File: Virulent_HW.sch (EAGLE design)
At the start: 74 parts, among them SW1 COM08229, SW2 COM08720, U1 STM32F050G6U6

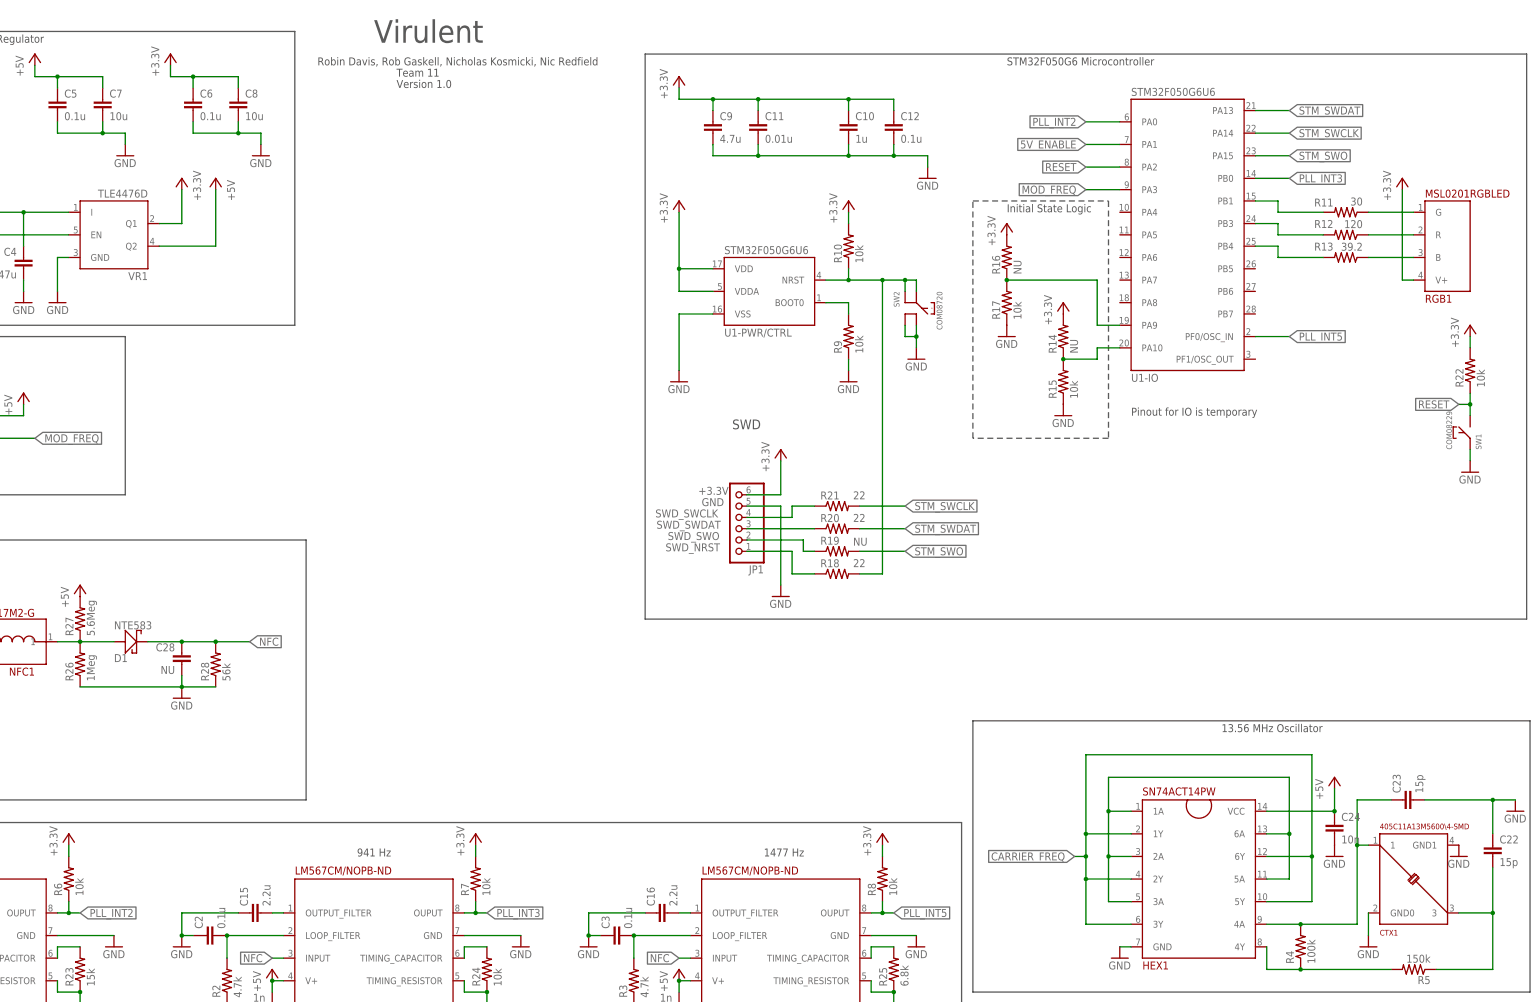
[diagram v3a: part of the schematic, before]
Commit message: Updated uC pinout.
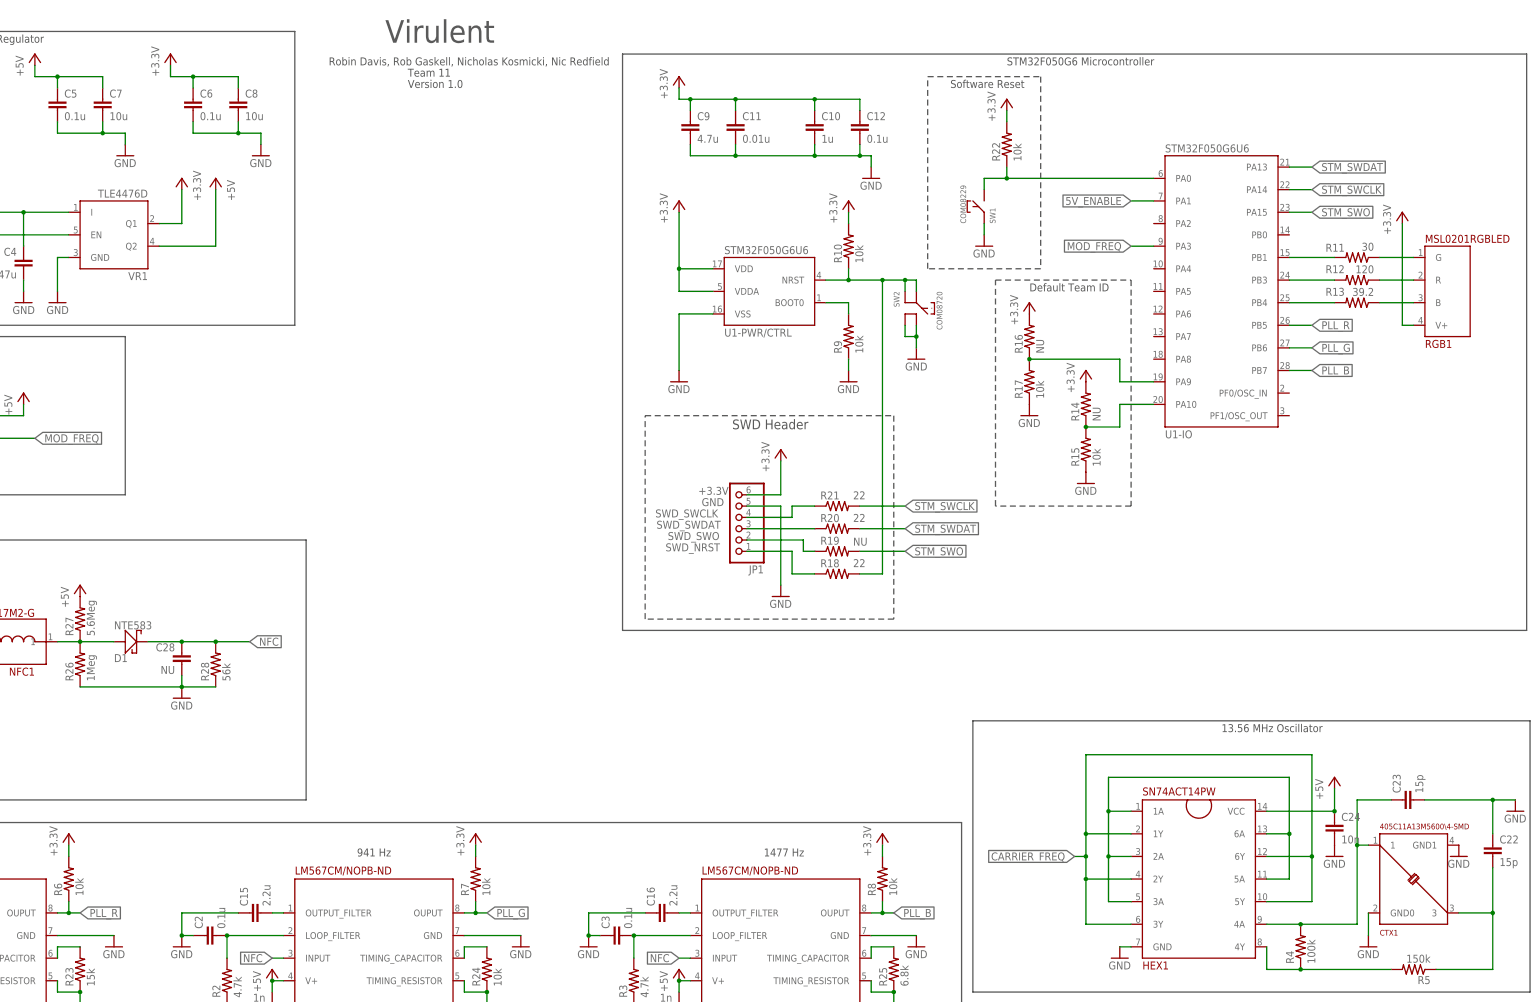
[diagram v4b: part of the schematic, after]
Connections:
- net N$11 renamed LED_GREEN
- net N$15 renamed LED_RED
- net N$16 renamed LED_BLUE
- net N$21 renamed O_GREEN
- net N$22 renamed O_RED
- net N$23 renamed O_BLUE
- net N$25 renamed TEAMID1
- net N$28 renamed TEAMID0
- removed net PLL_INT2: PLL1.OUPUT@8, R6.1, U1-IO.PA0@6
- removed net PLL_INT3: PLL2.OUPUT@8, R7.1, U1-IO.PB0@14
- removed net PLL_INT5: PLL3.OUPUT@8, R8.1, U1-IO.PF0/OSC_IN@2
- removed net RESET: R22.1, SW1.2@2, U1-IO.PA2@8
- new net NRESET_SOFT: R22.1, SW1.2@2, U1-IO.PA0@6
- new net PLL_B: PLL3.OUPUT@8, R8.1, U1-IO.PB7@28
- new net PLL_G: PLL2.OUPUT@8, R7.1, U1-IO.PB6@27
- new net PLL_R: PLL1.OUPUT@8, R6.1, U1-IO.PB5@26
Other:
- note added: "Default Team ID"
- note added: "SWD Header"
- note added: "Software Reset"
- note removed: "Initial State Logic"
- note removed: "Pinout for IO is temporary"
- note removed: "SWD"
- moved on the sheet: C10, C11, C12, C9, R11, R12, R13, R14, R15, R16, R17, R22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

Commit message: updated cap sizes. Started to mess with board layour but did not accomplish very much.
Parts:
- added C30: 0.1u, rcl:C-EUC0402
- added R31: 10k, Virulent_HW:R-US_R0402
- C1, C14, C15, C16, C17, C18, C19, C2, C20, C21, C22, C23, C24, C25, C27, C28, C29, C3: device rcl:C-EUC1206 -> rcl:C-EUC0402
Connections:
- removed net CARRIER_FREQ: HEX1.1Y@2, HEX1.2Y@4, HEX1.3Y@6, HEX1.5Y@10, HEX1.6Y@12, SPST1.A@1
- new net CHOPPED_FREQ: C24.1, HEX1.VCC@14, SPST1.B@2
- new net N$11: C30.2, SPST1.VCC@5
- net +5V: now also C30.1, SPST1.A@1; no longer C24.1, HEX1.VCC@14, SPST1.VCC@5
- net 5V_ENABLE: now also R31.2
- net GND: now also R31.1
- net NFC: now also HEX1.1Y@2, HEX1.2Y@4, HEX1.3Y@6, HEX1.5Y@10, HEX1.6Y@12; no longer SPST1.B@2
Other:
- note added: "Frequency Generation"
- note added: "NFC"
- note removed: "13.56 MHz Oscillator"
- note removed: "Frequency Modulation"
- note removed: "Receiver"
- moved on the sheet: C10, C11, C12, C22, C23, C24, C25, C28, C29, C9, CT1, CTX1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

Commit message: messed around with PCB layout
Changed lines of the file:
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@@
 <pinref part="R5" gate="G$1" pin="2"/>
 <wire x1="88.9" y1="114.3" x2="109.22" y2="114.3" width="0.1524" layer="91"/>
+<junction x="109.22" y="127"/>
 </segment>
 </net>
@@
 <pinref part="C24" gate="G$1" pin="1"/>
 <wire x1="48.26" y1="162.56" x2="101.6" y2="162.56" width="0.1524" layer="91"/>
-</segment>
-</net>
+<junction x="101.6" y="162.56"/>
+</segment>
+</net>

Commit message: First Draft of PCB. Changes made to reciever of schematic per Nic's instructions.Changed LED pins to better suit routing needs. Added dpdt switch to change nfc coil from tx/rx, to be controlled by microcontroller. Added user's momentary push-button
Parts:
- removed D1: NTE583, Virulent_HW:NTE583
- added C31, C35: 1n, rcl:C-EUC0402
- added C32, C33, C34: 470n, rcl:C-EUC0402
- added H1, H2: MOUNT-HOLE3.2, holes:MOUNT-HOLE3.2
- added R30: 10k, Virulent_HW:R-US_R0402
- added SW3: BUTTON, Virulent_HW:BUTTON
- added T1, T2: (no value), transistor:2N2222-NPN-TO18-EBC
- added TP9, TPGND, TP_+3.3V, TP_+5V, TP_13.56M, TP_5V_ENABLE, TP_9V, TP_CHOP_IN, TP_CHOP_OUT, TP_GND, TP_TX_OUT: TPTP06SQ, testpad:TPTP06SQ
- added U2: MAX14536, Virulent_HW:MAX14536
- R26: value 1Meg -> 150k
- R27: value 5.6Meg -> 100k
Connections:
- net TEAMID0 renamed N$34
- removed net LED_BLUE: R13.1, RGB1.B@3
- removed net LED_GREEN: R11.1, RGB1.G@1
- removed net LED_RED: R12.1, RGB1.R@2
- removed net N$11: C30.2, SPST1.VCC@5
- removed net NFC: C28.1, D1.CATHODE@2, HEX1.1Y@2, HEX1.2Y@4, HEX1.3Y@6, HEX1.5Y@10, HEX1.6Y@12, PLL1.INPUT@3, PLL2.INPUT@3, PLL3.INPUT@3, R28.2
- removed net O_BLUE: R13.2, U1-IO.PB4@25
- removed net O_GREEN: R11.2, U1-IO.PB1@15
- removed net O_RED: R12.2, U1-IO.PB3@24
- new net +2V: C31.1, R26.1, R27.2, T1.C, T2.B, U2.NO2@3
- new net N$16: C32.2, PLL1.INPUT@3
- new net N$20: C25.2, CT1.B@2, U2.COM1@9
- new net N$21: R11.1, RGB1.B@3
- new net N$22: T1.B, T2.C, U2.NO1@10
- new net N$23: C34.2, PLL2.INPUT@3
- new net N$25: C33.2, PLL3.INPUT@3
- new net N$28: R11.2, U1-IO.PA5@11
- new net N$31: R12.2, U1-IO.PA7@13
- new net N$32: NFC1.1@1, U2.COM2@4
- new net N$35: R12.1, RGB1.G@1
- new net N$36: R13.1, RGB1.R@2
- new net RX_OUT: C28.1, C32.1, C33.1, C34.1, R28.2, T1.E, T2.E, TP9.TP
- new net TRIGGER: R30.1, SW3.2@2, U1-IO.PA4@10
- new net TX/RX: U1-IO.PA2@8, U2.CB@1
- new net TX_OUT: HEX1.1Y@2, HEX1.2Y@4, HEX1.3Y@6, HEX1.5Y@10, HEX1.6Y@12, TP_TX_OUT.TP, U2.NC2@5
- net +3.3V: now also R30.2, TP_+3.3V.TP
- net +5V: now also C35.2, R26.2, SPST1.VCC@5, TP_+5V.TP, U2.EN@2, U2.VCC@7; no longer R27.2
- net +9-36V: now also TP_9V.TP
- net 5V_ENABLE: now also TP_5V_ENABLE.TP
- net CHOPPED_FREQ: now also TP_CHOP_OUT.TP
- net GND: now also C30.2, C31.2, C35.1, R27.1, SW3.1@1, TPGND.TP, TP_GND.TP, U2.GND@6, U2.NC1@8; no longer C25.2, CT1.B@2, R26.1
- net MOD_FREQ: now also TP_CHOP_IN.TP
- net N$18: now also TP_13.56M.TP
- net N$29: now also R13.2, U1-IO.PA6@12; no longer D1.ANNODE@1, NFC1.1@1, R26.2, R27.1
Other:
- note removed: "Frequency Generation"
- moved on the sheet: C1, C2, C20, C21, C22, C23, C24, C25, C26, C28, C29, C3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

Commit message: minor changes made to schematic for primarily esthetic reasons. Changed Version number to 2.0
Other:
- note added: "Frequency Generation"
- note added: "NFC Antenna and Tuner"
- note added: "Reciever Circuitry"
- note added: "Tx/Rx Switch"
- note added: "Version 2.0"
- note removed: "NFC"
- note removed: "Version 1.0"
- moved on the sheet: C22, C23, C24, C25, C28, C29, C30, C31, C35, CT1, CTX1, H1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
